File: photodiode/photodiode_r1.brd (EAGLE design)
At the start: 27.9 x 53.3 mm, 34 parts, among them M12_TUBE_MOUNT PT-LH001, U10 MIC5225, U11 AD829, U12 MIC5270, U9 ADA4899

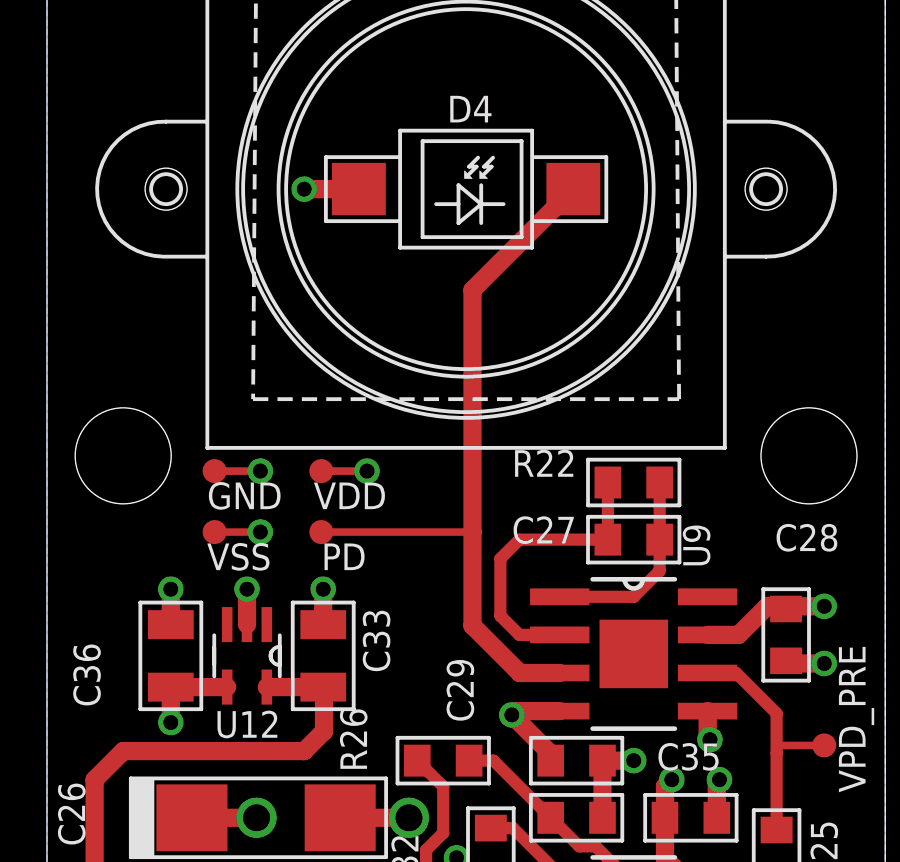
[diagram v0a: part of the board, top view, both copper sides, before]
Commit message: Modifications to photodiode circuit.
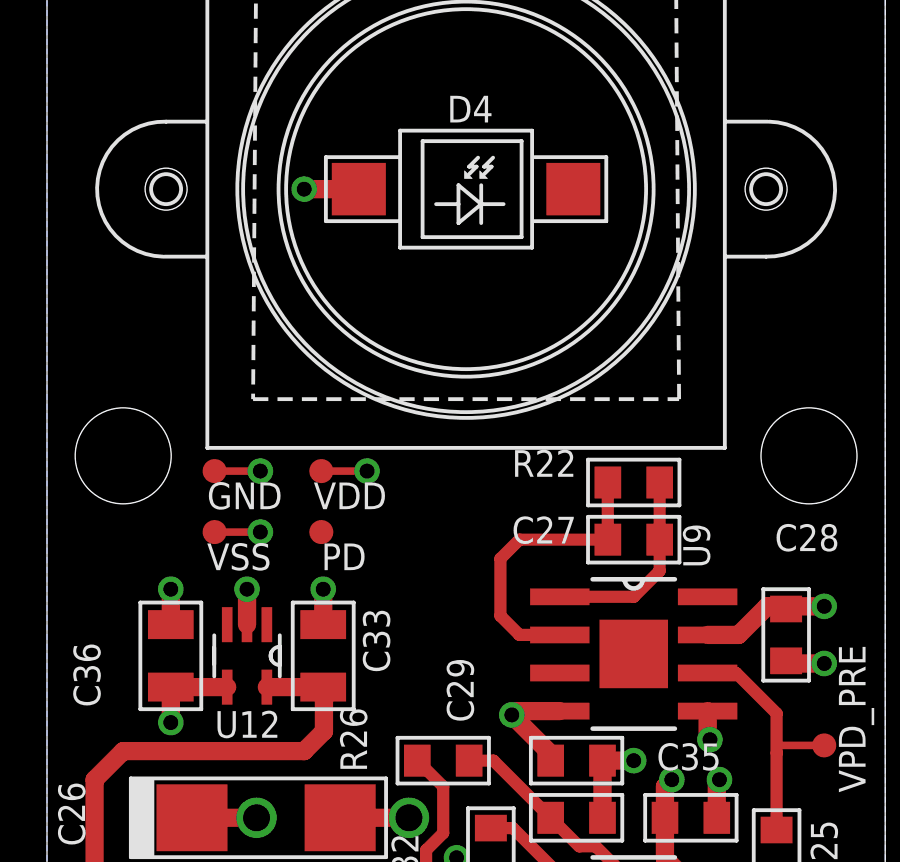
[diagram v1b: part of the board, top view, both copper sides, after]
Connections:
- removed net N$19: D4.C, PD.TP, U9.3
- new net AGND: U9.3
- net N$17: now also D4.C, PD.TP
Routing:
- net N$19: track 24.5 -> 0.00 mm
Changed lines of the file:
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@@
 <wire x1="24.003" y1="46.482" x2="24.638" y2="47.117" width="0.4064" layer="1"/>
 <wire x1="24.638" y1="47.117" x2="27.5844" y2="47.117" width="0.4064" layer="1"/>
-</signal>
-<signal name="N$19">
 <contactref element="D4" pad="C"/>
-<contactref element="U9" pad="3"/>
-<wire x1="26.435" y1="58.801" x2="23.0736875" y2="55.4396875" width="0.6096" layer="1"/>
-<wire x1="23.0736875" y1="55.4396875" x2="23.0736875" y2="47.371" width="0.6096" layer="1"/>
-<wire x1="23.0736875" y1="47.371" x2="23.0736875" y2="44.24951875" width="0.6096" layer="1"/>
-<wire x1="23.0736875" y1="44.24951875" x2="24.65120625" y2="42.672" width="0.6096" layer="1"/>
-<wire x1="24.65120625" y1="42.672" x2="25.9842" y2="42.672" width="0.6096" layer="1"/>
 <contactref element="PD" pad="TP"/>
-<wire x1="18.034" y1="47.371" x2="23.0736875" y2="47.371" width="0.254" layer="1"/>
+<wire x1="27.5844" y1="49.022" x2="26.435" y2="58.801" width="0" layer="19" extent="1-1"/>
+<wire x1="18.034" y1="47.371" x2="24.003" y2="46.482" width="0" layer="19" extent="1-1"/>
 </signal>
 <signal name="+7V">
@@
 <signal name="N$30">
 </signal>
+<signal name="AGND">
+<contactref element="U9" pad="3"/>
+</signal>
 </signals>

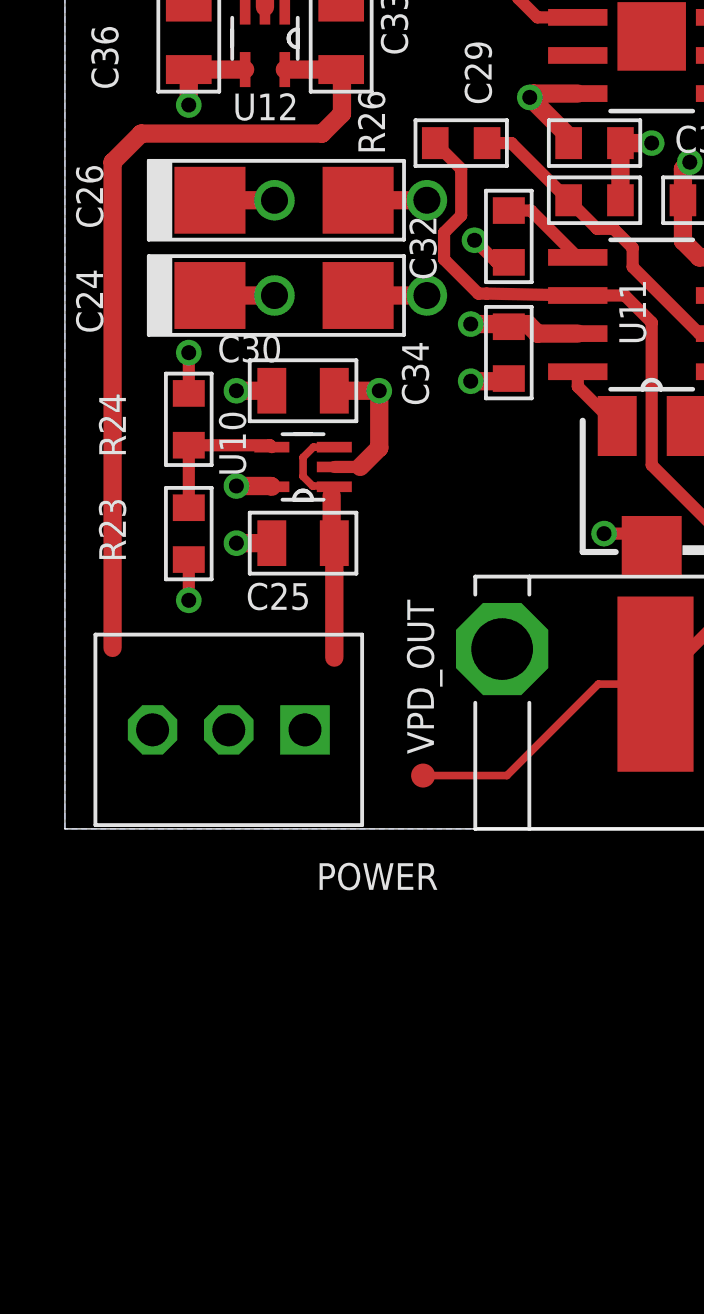
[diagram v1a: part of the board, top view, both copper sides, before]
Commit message: Added some components for the photodiode. Fixed up power supply rails for driver.
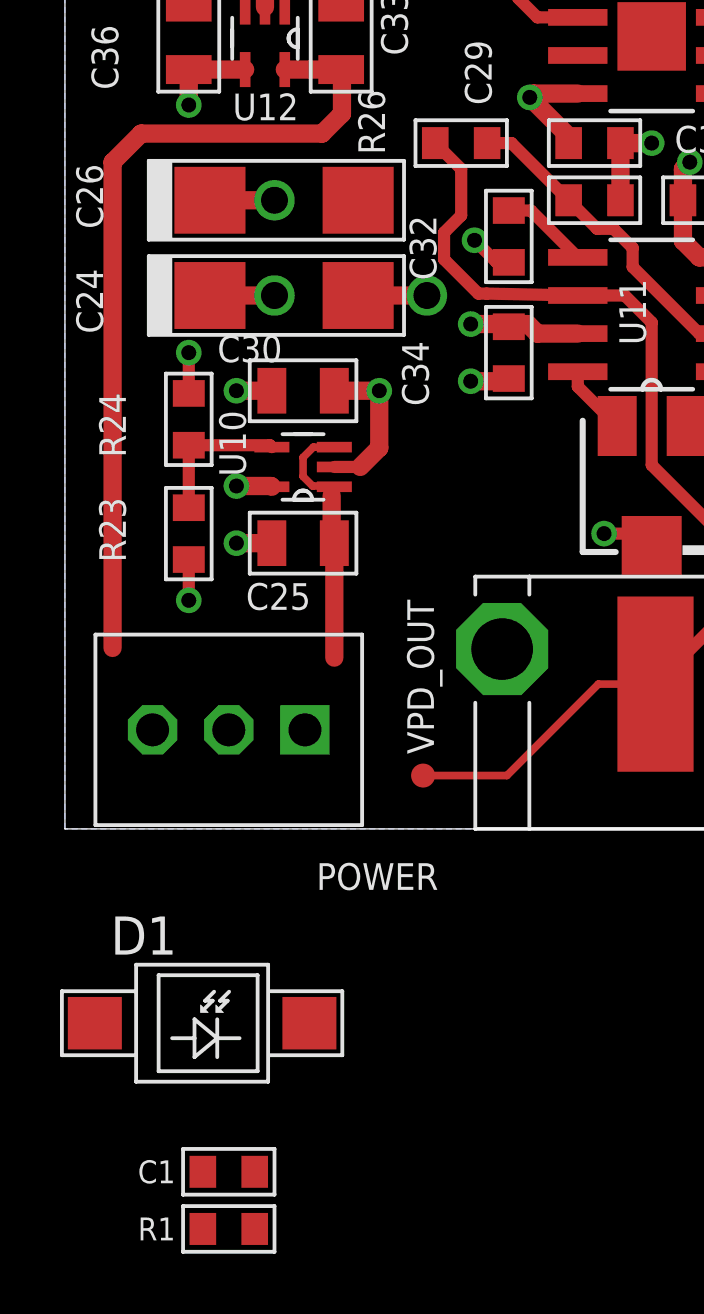
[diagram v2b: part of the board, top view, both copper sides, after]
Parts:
- added C1: .1uF, cyclops:0603
- added D1: VBPW34S, cyclops:VBPW34S
- added R1: 20k, cyclops:0603
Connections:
- new net N$1: C1.1, D1.C, R1.2, U9.3
- net -5V: now also D1.A
- net AGND: now also C1.2, R1.1; no longer U9.3
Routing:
- net -5V: track 19.5 -> 17.2 mm, vias 8 -> 7
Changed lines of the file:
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@@
 <attribute name="VALUE" x="21.844" y="35.179" size="0.889" layer="27" font="vector" ratio="18" rot="R90" align="center-left"/>
+</element>
+<element name="D1" library="cyclops" package="VBPW34S" value="VBPW34S" x="13.462" y="10.414"/>
+<element name="C1" library="cyclops" package="0603" value=".1uF" x="14.351" y="5.461"/>
+<element name="R1" library="cyclops" package="0603" value="20k" x="14.351" y="3.556">
+<attribute name="MN" value="Panasonic" x="14.351" y="3.556" size="1.778" layer="27" display="off"/>
+<attribute name="DK" value="PxxxxHTR-ND" x="14.351" y="3.556" size="1.778" layer="27" display="off"/>
+<attribute name="MPN" value="ERJ-3EKFxxxxV" x="14.351" y="3.556" size="1.778" layer="27" display="off"/>
 </element>
 </elements>
@@
 <via x="19.558" y="49.403" extent="1-16" drill="0.5"/>
 <wire x1="18.034" y1="49.403" x2="19.558" y2="49.403" width="0.254" layer="1"/>
+<wire x1="25.9842" y1="33.401" x2="30.9118" y2="43.942" width="0" layer="19" extent="1-1"/>
+<wire x1="15.875" y1="34.671" x2="22.4155" y2="33.7185" width="0" layer="19" extent="1-1"/>
+<wire x1="15.7861" y1="31.496" x2="15.875" y2="34.671" width="0" layer="19" extent="1-1"/>
+<wire x1="15.7607" y1="28.321" x2="15.7861" y2="31.496" width="0" layer="19" extent="1-1"/>
+<wire x1="13.0175" y1="25.8699" x2="14.605" y2="28.321" width="0" layer="19" extent="1-1"/>
+<wire x1="19.558" y1="49.403" x2="30.9118" y2="43.942" width="0" layer="19" extent="1-1"/>
 </signal>
 <signal name="VPD_PRE">
@@
 <contactref element="D4" pad="A"/>
 <wire x1="19.285" y1="58.801" x2="17.4625" y2="58.801" width="0.6096" layer="1"/>
-<via x="20.955" y="37.846" extent="1-16" drill="0.9" shape="octagon"/>
-<contactref element="C26" pad="-"/>
-<wire x1="18.6625" y1="37.846" x2="20.955" y2="37.846" width="0.6096" layer="1"/>
 <via x="29.718" y="39.116" extent="1-16" drill="0.5"/>
 <via x="24.384" y="41.275" extent="1-16" drill="0.5"/>
@@
 <wire x1="26.8605" y1="26.7335" x2="28.0355" y2="26.7335" width="0.4064" layer="1"/>
 <wire x1="28.0355" y1="26.7335" x2="28.448" y2="26.321" width="0.4064" layer="1"/>
+<contactref element="D1" pad="A"/>
+<contactref element="C26" pad="-"/>
+<wire x1="16.002" y1="47.371" x2="17.4625" y2="58.801" width="0" layer="19" extent="1-1"/>
+<wire x1="14.8971" y1="42.2021" x2="14.478" y2="47.371" width="0" layer="19" extent="1-1"/>
+<wire x1="18.6625" y1="37.846" x2="14.8971" y2="42.2021" width="0" layer="19" extent="1-1"/>
+<wire x1="24.384" y1="41.275" x2="18.6625" y2="37.846" width="0" layer="19" extent="1-1"/>
+<wire x1="29.4894" y1="38.8874" x2="25.6794" y2="39.751" width="0" layer="19" extent="1-1"/>
+<wire x1="30.988" y1="40.4495" x2="29.718" y2="39.116" width="0" layer="19" extent="1-1"/>
+<wire x1="28.0355" y1="26.7335" x2="30.0355" y2="35.941" width="0" layer="19" extent="1-1"/>
+<wire x1="9.887" y1="10.414" x2="26.8605" y2="26.7335" width="0" layer="19" extent="1-1"/>
 </signal>
 <signal name="N$18">
@@
 <signal name="N$30">
 </signal>
+<signal name="N$1">
+<contactref element="D1" pad="C"/>
+<contactref element="U9" pad="3"/>
+<contactref element="C1" pad="1"/>
+<contactref element="R1" pad="2"/>
+<wire x1="17.037" y1="10.414" x2="25.9842" y2="42.672" width="0" layer="19" extent="1-1"/>
+<wire x1="13.4874" y1="5.461" x2="17.037" y2="10.414" width="0" layer="19" extent="1-1"/>
+<wire x1="15.2146" y1="3.556" x2="13.4874" y2="5.461" width="0" layer="19" extent="1-1"/>
+</signal>
 <signal name="AGND">
-<contactref element="U9" pad="3"/>
+<contactref element="C1" pad="2"/>
+<contactref element="R1" pad="1"/>
+<wire x1="13.4874" y1="3.556" x2="15.2146" y2="5.461" width="0" layer="19" extent="1-1"/>
 </signal>
 </signals>
